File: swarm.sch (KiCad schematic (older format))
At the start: 1 part, among them U1 STM32F103RETx

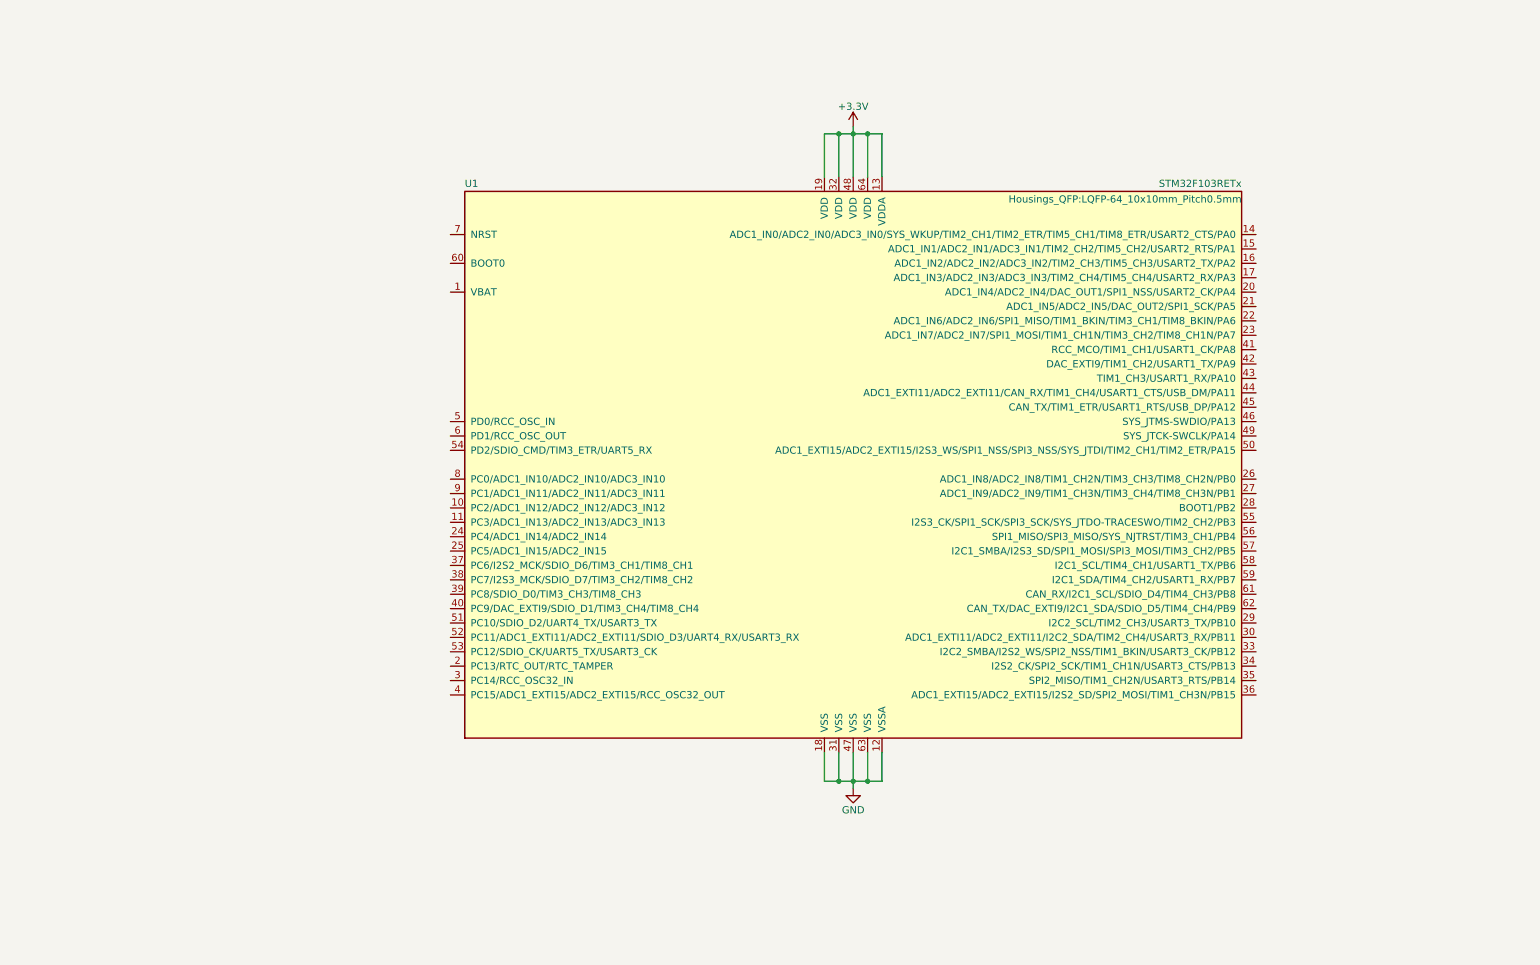
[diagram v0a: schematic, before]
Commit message: Adds decouplings capacitors
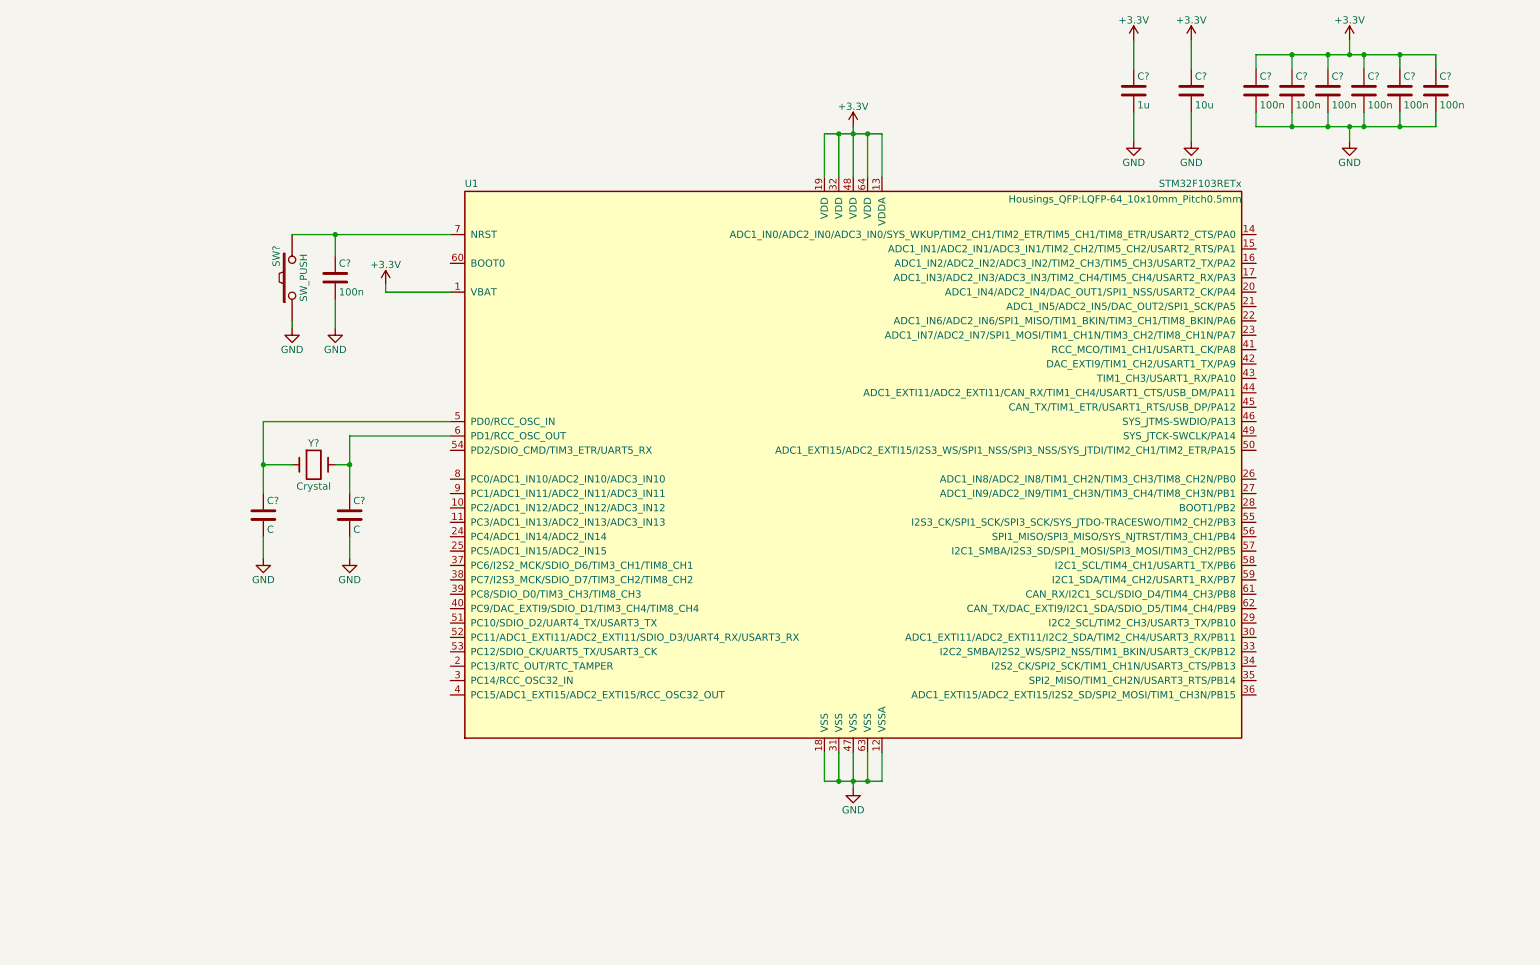
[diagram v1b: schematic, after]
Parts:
- added C? (x7): 100n, symbol C
- added C?: 10u, symbol C
- added C?: 1u, symbol C
- added C? (x2): C, symbol C
- added SW?: SW_PUSH, symbol SW_PUSH
- added Y?: Crystal, symbol Crystal
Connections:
- net +3V3: now also U1.1 (VBAT), C?.1, C?.1, C?.1, C?.1, C?.1, C?.1, C?.1, C?.1
- net GND: now also C?.2, C?.2, C?.2, C?.2, C?.2, C?.2, C?.2, C?.2, C?.2, C?.2, C?.2, SW?.1
- net at U1.5 (PD0/RCC_OSC_IN): now also C?.1, Y?.1
- net at U1.6 (PD1/RCC_OSC_OUT): now also C?.1, Y?.2
- net at U1.7 (NRST): now also C?.1, SW?.2

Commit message: Adds power sypply based on proven LM3671MF-3.3
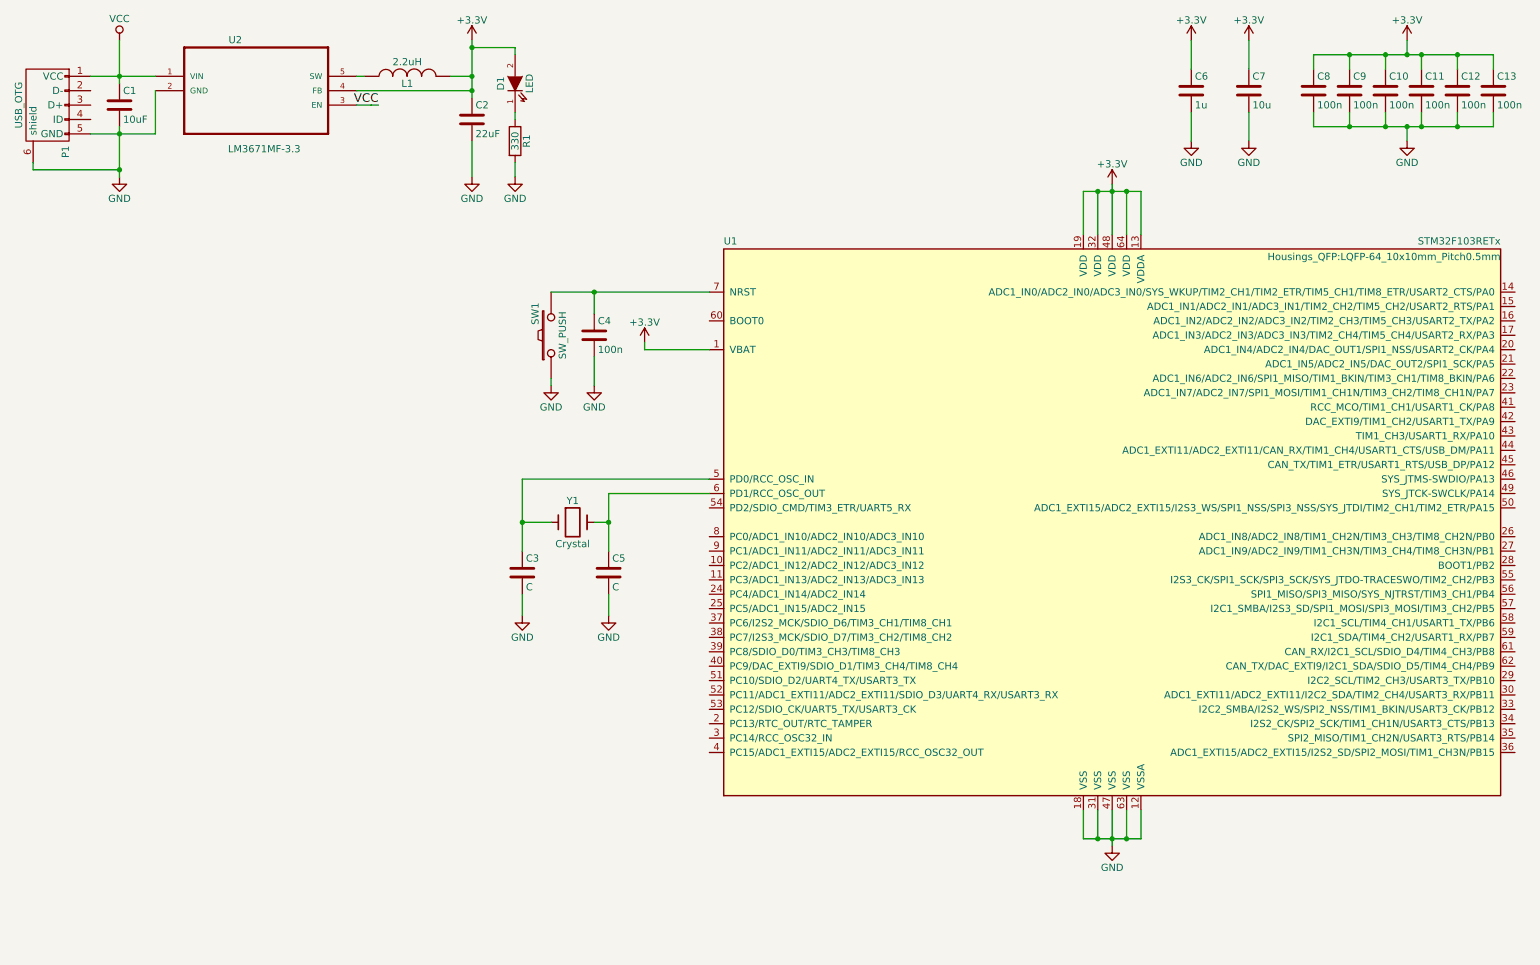
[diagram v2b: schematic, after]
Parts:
- added C1: 10uF, Capacitors_SMD:C_1206, symbol C
- added C2: 22uF, Capacitors_SMD:C_1206, symbol C
- added D1: LED, LEDs:LED_1206, symbol LED
- added L1: 2.2uH, Inductors:Inductor_Taiyo-Yuden_NR-24xx_HandSoldering, symbol INDUCTOR
- added P1: USB_OTG, Connect:USB_Mini-B, symbol USB_OTG
- added R1: 330, Resistors_SMD:R_1206, symbol R
- added U2: LM3671MF-3.3, TO_SOT_Packages_SMD:SOT-23-5, symbol LM3671MF-3.3
- gave numbers to parts that had none: 13
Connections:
- net +3V3: now also C2.1, D1.2 (A), L1.2, U2.4 (FB)
- net GND: now also C1.2, C2.2, P1.5 (GND), P1.6 (shield), R1.2, U2.2 (GND)
- new net: L1.1, U2.5 (SW)
- new net: D1.1 (K), R1.1
- new net VCC: C1.1, P1.1 (VCC), U2.1 (VIN), U2.3 (EN)
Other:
- moved on the sheet: C10, C11, C12, C13, C3, C4, C5, C6, C7, C8, C9, SW1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

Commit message: Updates netlist, footprint selection
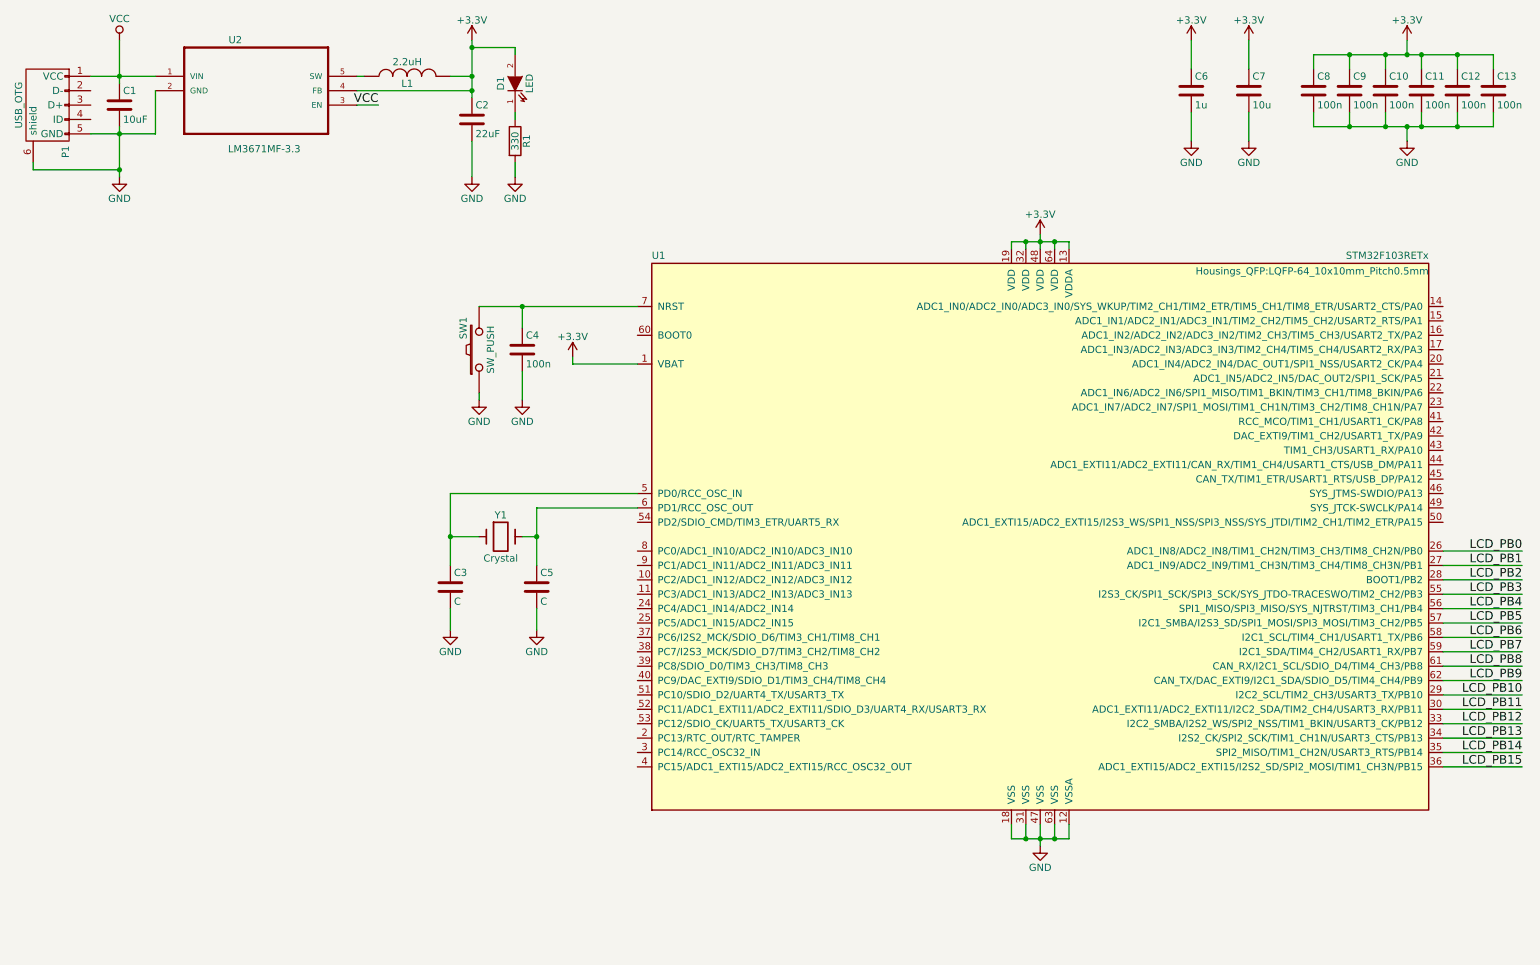
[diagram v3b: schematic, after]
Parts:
- C1, C2: footprint Capacitors_SMD:C_1206 -> Capacitors_SMD:C_1206_HandSoldering
- C10, C11, C12, C13, C3, C4, C5, C6, C7, C8, C9: footprint (none) -> Capacitors_SMD:C_1206_HandSoldering
- SW1: footprint (none) -> Buttons_Switches_SMD:SW_SPST_PTS645
- Y1: footprint (none) -> Crystals:Crystal_SMD_5032_2Pads
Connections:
- net LCD_PB0: now reaches U1.26 (ADC1_IN8/ADC2_IN8/TIM1_CH2N/TIM3_CH3/TIM8_CH2N/PB0)
- net LCD_PB1: now reaches U1.27 (ADC1_IN9/ADC2_IN9/TIM1_CH3N/TIM3_CH4/TIM8_CH3N/PB1)
- net LCD_PB2: now reaches U1.28 (BOOT1/PB2)
- net LCD_PB10: now reaches U1.29 (I2C2_SCL/TIM2_CH3/USART3_TX/PB10)
- net LCD_PB11: now reaches U1.30 (ADC1_EXTI11/ADC2_EXTI11/I2C2_SDA/TIM2_CH4/USART3_RX/PB11)
- net LCD_PB12: now reaches U1.33 (I2C2_SMBA/I2S2_WS/SPI2_NSS/TIM1_BKIN/USART3_CK/PB12)
- net LCD_PB13: now reaches U1.34 (I2S2_CK/SPI2_SCK/TIM1_CH1N/USART3_CTS/PB13)
- net LCD_PB14: now reaches U1.35 (SPI2_MISO/TIM1_CH2N/USART3_RTS/PB14)
- net LCD_PB15: now reaches U1.36 (ADC1_EXTI15/ADC2_EXTI15/I2S2_SD/SPI2_MOSI/TIM1_CH3N/PB15)
- net LCD_PB3: now reaches U1.55 (I2S3_CK/SPI1_SCK/SPI3_SCK/SYS_JTDO-TRACESWO/TIM2_CH2/PB3)
- net LCD_PB4: now reaches U1.56 (SPI1_MISO/SPI3_MISO/SYS_NJTRST/TIM3_CH1/PB4)
- net LCD_PB5: now reaches U1.57 (I2C1_SMBA/I2S3_SD/SPI1_MOSI/SPI3_MOSI/TIM3_CH2/PB5)
- net LCD_PB6: now reaches U1.58 (I2C1_SCL/TIM4_CH1/USART1_TX/PB6)
- net LCD_PB7: now reaches U1.59 (I2C1_SDA/TIM4_CH2/USART1_RX/PB7)
- net LCD_PB8: now reaches U1.61 (CAN_RX/I2C1_SCL/SDIO_D4/TIM4_CH3/PB8)
- net LCD_PB9: now reaches U1.62 (CAN_TX/DAC_EXTI9/I2C1_SDA/SDIO_D5/TIM4_CH4/PB9)
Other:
- moved on the sheet: C3, C4, C5, SW1, U1, Y1

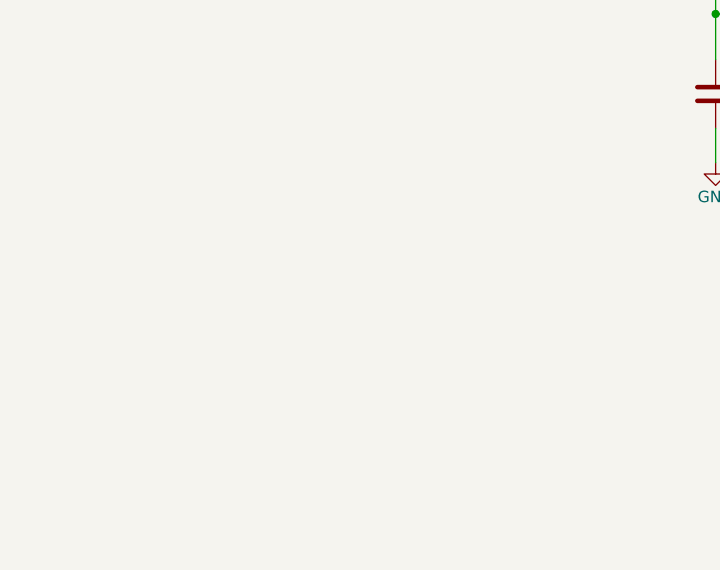
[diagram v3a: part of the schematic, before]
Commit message: Adds MicroSD card and Mini USB connector via volium KiCad library
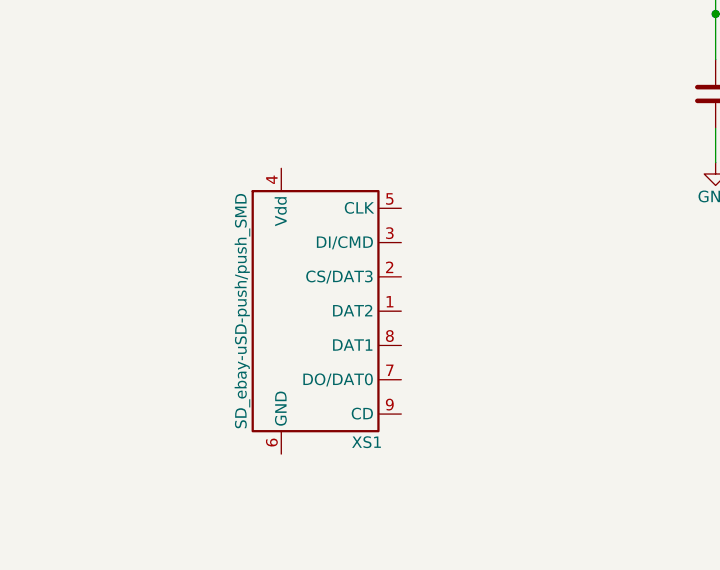
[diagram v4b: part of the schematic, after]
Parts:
- added XS1: SD_ebay-uSD-push/push_SMD, volium:Conn_uSDcard, symbol SD_ebay-uSD-push/push_SMD
- P1: footprint Connect:USB_Mini-B -> volium:USB_Mini-B
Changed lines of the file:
@@
 F 0 "P1" H 1225 1075 50  0000 C CNN
 F 1 "USB_OTG" H 900 1400 50  0000 C CNN
-F 2 "Connect:USB_Mini-B" V 850 1100 50  0001 C CNN
+F 2 "volium:USB_Mini-B" V 850 1100 50  0001 C CNN
 F 3 "" V 850 1100 50  0000 C CNN
 	1    900  1200
@@
 Text Label 11150 5800 2    60   ~ 0
 LCD_PB15
+$Comp
+L SD_ebay-uSD-push/push_SMD XS1
+U 1 1 5840E1A5
+P 1950 5500
+F 0 "XS1" H 2175 4925 50  0000 C CNN
+F 1 "SD_ebay-uSD-push/push_SMD" V 1625 5500 50  0000 C CNN
+F 2 "volium:Conn_uSDcard" H 1950 5550 10  0001 C CNN
+F 3 "https://wiki.microduino.cc/images/c/ca/MicroSD.pdf" H 1950 5440 10  0001 C CNN
+F 4 "_" H 1950 5410 10  0001 C CNN "Manf#"
+F 5 "ebay" H 1950 5500 10  0001 C CNN "Manf"
+	1    1950 5500
+	1    0    0    -1
+$EndComp
 $EndSCHEMATC
